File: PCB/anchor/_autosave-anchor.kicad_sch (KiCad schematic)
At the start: 15 parts, among them J1 Conn_ARM_SWD_TagConnect_TC203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, J2 Conn_ARM_JTAG_SWD_10, J3 SM02B-SRSS-TB LFSN, U1 Voltage Regulator, U2 DWM3001C UWB, U3 LYR998

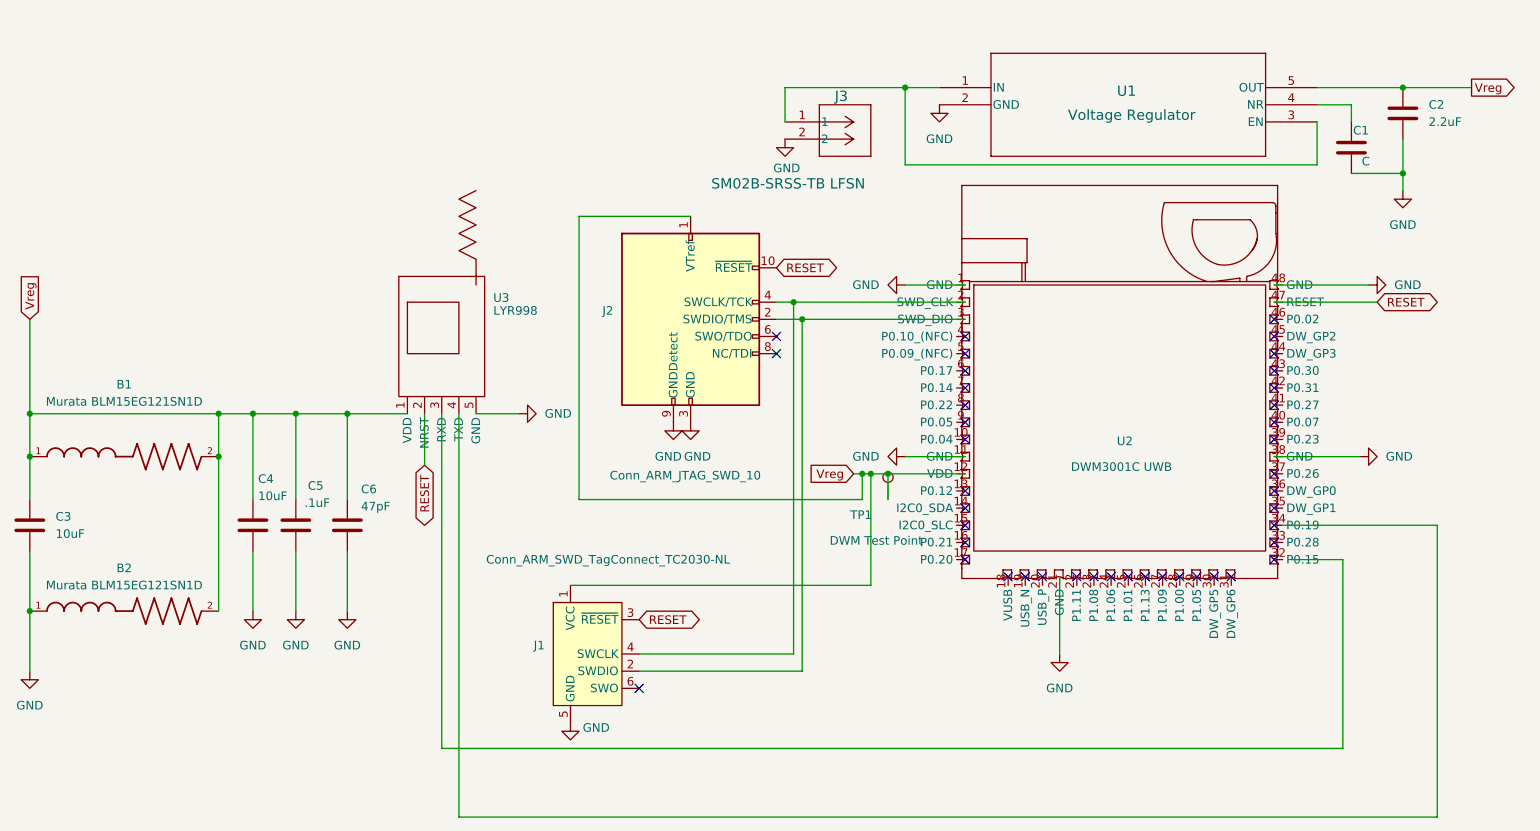
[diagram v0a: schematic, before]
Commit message: updated anchor pcb + DWM Datasheet
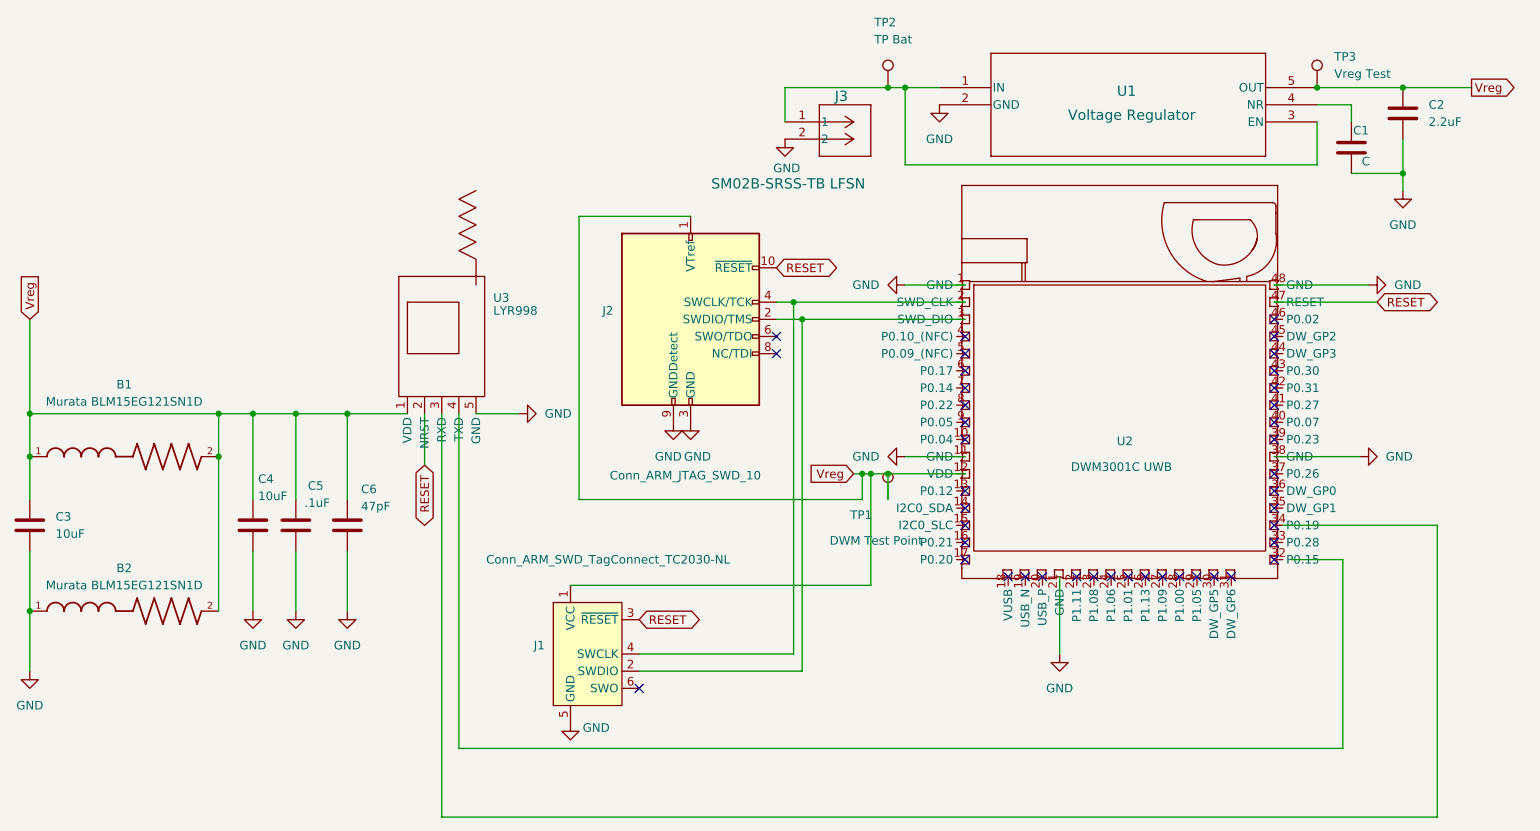
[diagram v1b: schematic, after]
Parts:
- added TP2: TP Bat, symbol Connector:TestPoint
- added TP3: Vreg Test, symbol Connector:TestPoint
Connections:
- net Vreg: now also TP3.1
- net at J3.1, U1.1 (IN), U1.3 (EN): now also TP2.1
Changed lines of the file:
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@@
 	(paper "A4")
 	(junction
+		(at 142.24 46.99)
+		(diameter 0)
+		(color 0 0 0 0)
+	)
+	(junction
 		(at 218.44 59.69)
 		(diameter 0)
@@
 	)
 	(junction
+		(at 205.74 46.99)
+		(diameter 0)
+		(color 0 0 0 0)
+	)
+	(junction
 		(at 139.7 104.14)
 		(diameter 0)
@@
 	(wire
 		(pts
-			(xy 127 46.99) (xy 144.78 46.99)
+			(xy 127 46.99) (xy 142.24 46.99)
 		)
 		(stroke
@@
 	(wire
 		(pts
-			(xy 209.55 144.78) (xy 76.2 144.78)
+			(xy 209.55 144.78) (xy 78.74 144.78)
 		)
 		(stroke
@@
 	(wire
 		(pts
+			(xy 76.2 154.94) (xy 223.52 154.94)
+		)
+		(stroke
+			(width 0)
+			(type default)
+		)
+	)
+	(wire
+		(pts
 			(xy 218.44 54.61) (xy 218.44 59.69)
 		)
@@
 	(wire
 		(pts
-			(xy 76.2 95.25) (xy 76.2 144.78)
-		)
-		(stroke
-			(width 0)
-			(type default)
-		)
-	)
-	(wire
-		(pts
 			(xy 15.24 81.28) (xy 15.24 95.25)
 		)
@@
 	(wire
 		(pts
-			(xy 223.52 154.94) (xy 78.74 154.94)
+			(xy 78.74 95.25) (xy 78.74 144.78)
 		)
 		(stroke
@@
 	(wire
 		(pts
+			(xy 76.2 95.25) (xy 76.2 154.94)
+		)
+		(stroke
+			(width 0)
+			(type default)
+		)
+	)
+	(wire
+		(pts
 			(xy 54.61 95.25) (xy 54.61 107.95)
 		)
@@
 	(wire
 		(pts
+			(xy 142.24 46.99) (xy 144.78 46.99)
+		)
+		(stroke
+			(width 0)
+			(type default)
+		)
+	)
+	(wire
+		(pts
 			(xy 125.73 81.28) (xy 129.54 81.28)
 		)
@@
 	(wire
 		(pts
-			(xy 78.74 95.25) (xy 78.74 154.94)
-		)
-		(stroke
-			(width 0)
-			(type default)
-		)
-	)
-	(wire
-		(pts
 			(xy 15.24 95.25) (xy 15.24 101.6)
 		)
@@
 	)
 	(symbol
+		(lib_id "Connector:TestPoint")
+		(at 142.24 46.99 0)
+		(unit 1)
+		(exclude_from_sim no)
+		(in_bom yes)
+		(on_board yes)
+		(dnp no)
+		(property "Reference" "TP2"
+			(at 140.208 37.338 0)
+			(effects
+				(font
+					(size 1.27 1.27)
+				)
+				(justify left)
+			)
+		)
+		(property "Value" "TP Bat"
+			(at 140.208 39.878 0)
+			(effects
+				(font
+					(size 1.27 1.27)
+				)
+				(justify left)
+			)
+		)
+		(property "Footprint" ""
+			(at 147.32 46.99 0)
+			(effects
+				(font
+					(size 1.27 1.27)
+				)
+				(hide yes)
+			)
+		)
+		(property "Datasheet" "~"
+			(at 147.32 46.99 0)
+			(effects
+				(font
+					(size 1.27 1.27)
+				)
+				(hide yes)
+			)
+		)
+		(property "Description" "test point"
+			(at 142.24 46.99 0)
+			(effects
+				(font
+					(size 1.27 1.27)
+				)
+				(hide yes)
+			)
+		)
+		(pin "1"
+		)
+		(instances
+			(project ""
+				(path "/d60525eb-0f59-4f61-9b85-36ffaff6c19a"
+					(reference "TP2")
+					(unit 1)
+				)
+			)
+		)
+	)
+	(symbol
 		(lib_id "power:GND")
 		(at 127 54.61 0)
@@
 					(unit 1)
 				)
+			)
+		)
+	)
+	(symbol
+		(lib_id "Connector:TestPoint")
+		(at 205.74 46.99 0)
+		(unit 1)
+		(exclude_from_sim no)
+		(in_bom yes)
+		(on_board yes)
+		(dnp no)
+		(fields_autoplaced yes)
+		(property "Reference" "TP3"
+			(at 208.28 42.4179 0)
+			(effects
+				(font
+					(size 1.27 1.27)
+				)
+				(justify left)
+			)
+		)
+		(property "Value" "Vreg Test"
+			(at 208.28 44.9579 0)
+			(effects
+				(font
+					(size 1.27 1.27)
+				)
+				(justify left)
+			)
+		)
+		(property "Footprint" ""
+			(at 210.82 46.99 0)
+			(effects
+				(font
+					(size 1.27 1.27)
+				)
+				(hide yes)
+			)
+		)
+		(property "Datasheet" "~"
+			(at 210.82 46.99 0)
+			(effects
+				(font
+					(size 1.27 1.27)
+				)
+				(hide yes)
+			)
+		)
+		(property "Description" "test point"
+			(at 205.74 46.99 0)
+			(effects
+				(font
+					(size 1.27 1.27)
+				)
+				(hide yes)
+			)
+		)
+		(pin "1"
+		)
+		(instances
+			(project ""
+				(path "/d60525eb-0f59-4f61-9b85-36ffaff6c19a"
+					(reference "TP3")
+					(unit 1)
+				)
